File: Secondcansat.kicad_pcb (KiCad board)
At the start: 2 copper layers, 80 x 80 mm, 53 parts, among them IC1 XBP9B-XCWT-001, J1 OpenlogBreakout, J2 camerapower, J3 Pressure_MS5607, J4 Debugger, J5 light_sensor__SFH 7776, J6 CAM-M8Q-GPS, Q1 Q_PMOS_DGS, Q2 Q_NMOS_DGS, Q3 Q_NMOS_DGS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

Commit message: Finish PCB
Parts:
- moved C4 1.69 mm to (90.4, 107.1)
- moved L1 0.76 mm to (86.3, 108.3)
- moved C5 0.75 mm to (89.8, 109.1)
- moved L2 0.75 mm to (84.2, 108.3)
- moved C1 0.61 mm to (88.3, 111.4)
- moved R11 0.57 mm to (66.8, 85.4), turned to 0 degrees
- moved C2 0.38 mm to (88.5, 113.3)
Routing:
- net +3V3: track 0.00 -> 153.5 mm, vias 0 -> 6
- net +6V: track 0.00 -> 39.2 mm, vias 0 -> 3
- net SCL: track 0.00 -> 25.9 mm
- net SDA: track 0.00 -> 25.8 mm
- net TC_PD0: track 0.00 -> 17.7 mm, vias 0 -> 2
- net +5V: track 0.00 -> 15.8 mm
- net CSB: track 0.00 -> 13.6 mm
- net MCUVCC: track 0.00 -> 11.3 mm
- net Net-(C12-Pad2): track 0.00 -> 9.30 mm
- net MISO: track 0.00 -> 7.48 mm
- net Net-(C12-Pad1): track 0.00 -> 7.25 mm
- net SCLK: track 0.00 -> 6.83 mm
- net Net-(R1-Pad2): track 0.00 -> 6.37 mm
- net Net-(Q2-Pad3): track 0.00 -> 6.08 mm
- net PDICLK: track 0.00 -> 5.52 mm
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
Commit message: the real PCB
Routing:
- net GND: track 0.00 -> 124.5 mm, vias 0 -> 11
- net PDICLK: track 5.52 -> 61.4 mm, vias 0 -> 2
- net +6V: track 39.2 -> 90.6 mm, vias 3 -> 4
- net Therm_ADCA0: track 0.00 -> 47.7 mm, vias 0 -> 4
- net +3V3: track 153.5 -> 197.0 mm, vias 6 -> 7
- net PDIDATA: track 0.00 -> 38.2 mm, vias 0 -> 1
- net TX_PD7: track 0.00 -> 36.6 mm, vias 0 -> 2
- net RX_PD6: track 0.00 -> 33.3 mm, vias 0 -> 2
- net ADC_A1: track 0.00 -> 30.6 mm, vias 0 -> 2
- net MCUAVCC: track 4.50 -> 31.7 mm, vias 0 -> 2
- net SDA: track 25.8 -> 51.0 mm
- net PWM: track 1.63 -> 24.3 mm, vias 0 -> 2
- net MoterRIN1: track 1.88 -> 21.5 mm, vias 0 -> 2
- net MoterRIN2: track 0.00 -> 19.5 mm, vias 0 -> 2
- net MotorFIN1: track 0.00 -> 18.5 mm, vias 0 -> 2
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- added copper zone on B.Cu, net GND
- added copper zone on F.Cu, net GND

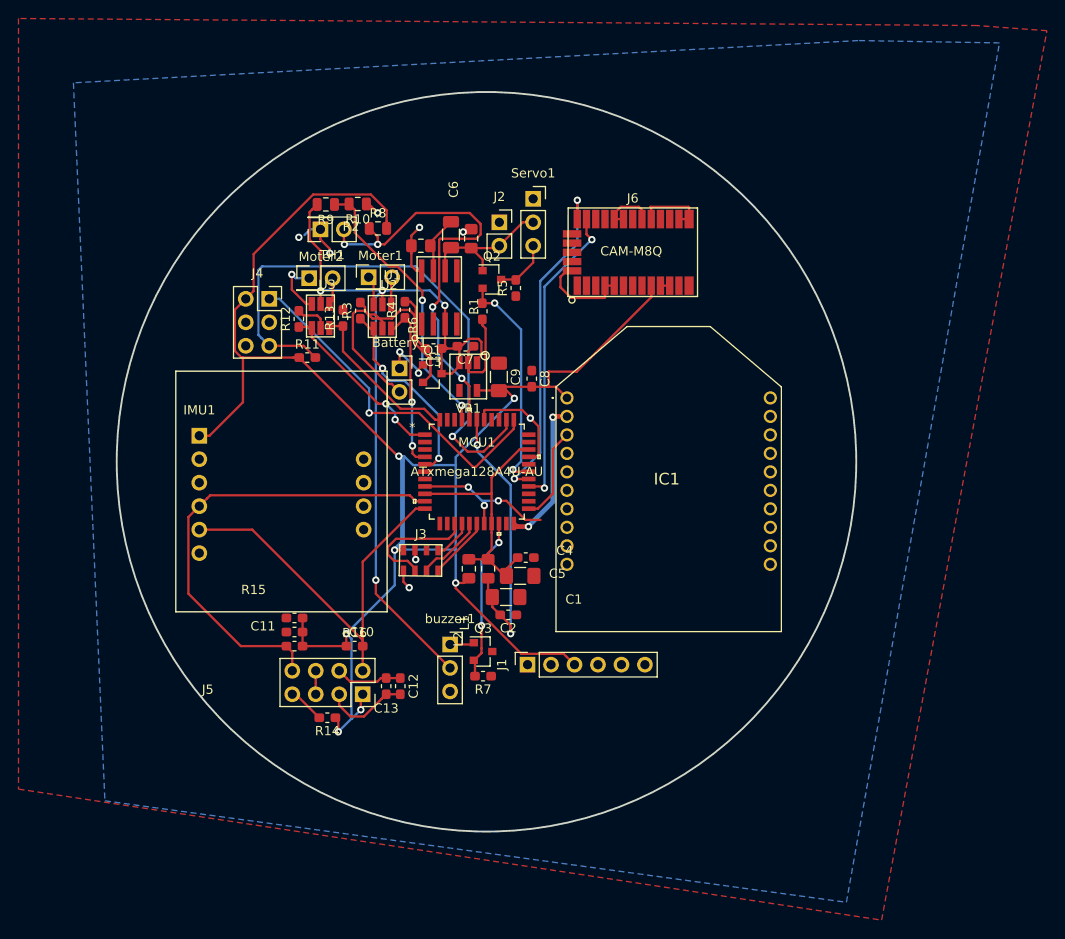
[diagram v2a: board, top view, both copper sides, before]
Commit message: moved reference values, added no fill zone and removed extra pin on moter
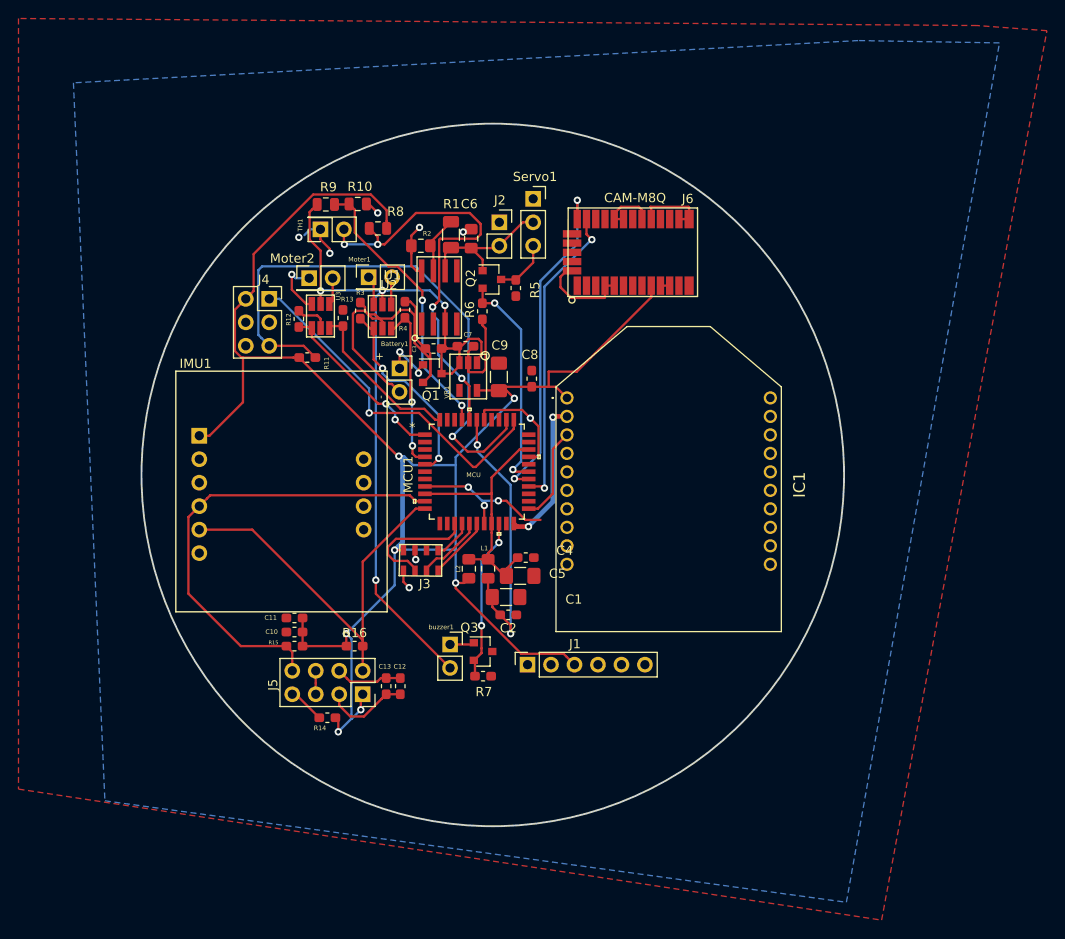
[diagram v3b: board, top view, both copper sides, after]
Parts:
- MCU1: value ATxmega128A4U-AU -> MCU
- buzzer1: footprint Connector_PinSocket_2.54mm:PinSocket_1x03_P2.54mm_Vertical -> Connector_PinSocket_2.54mm:PinSocket_1x02_P2.54mm_Vertical
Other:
- board size 80 x 80 mm -> 76 x 76 mm
- board text added: "+"
- board text added: "-"

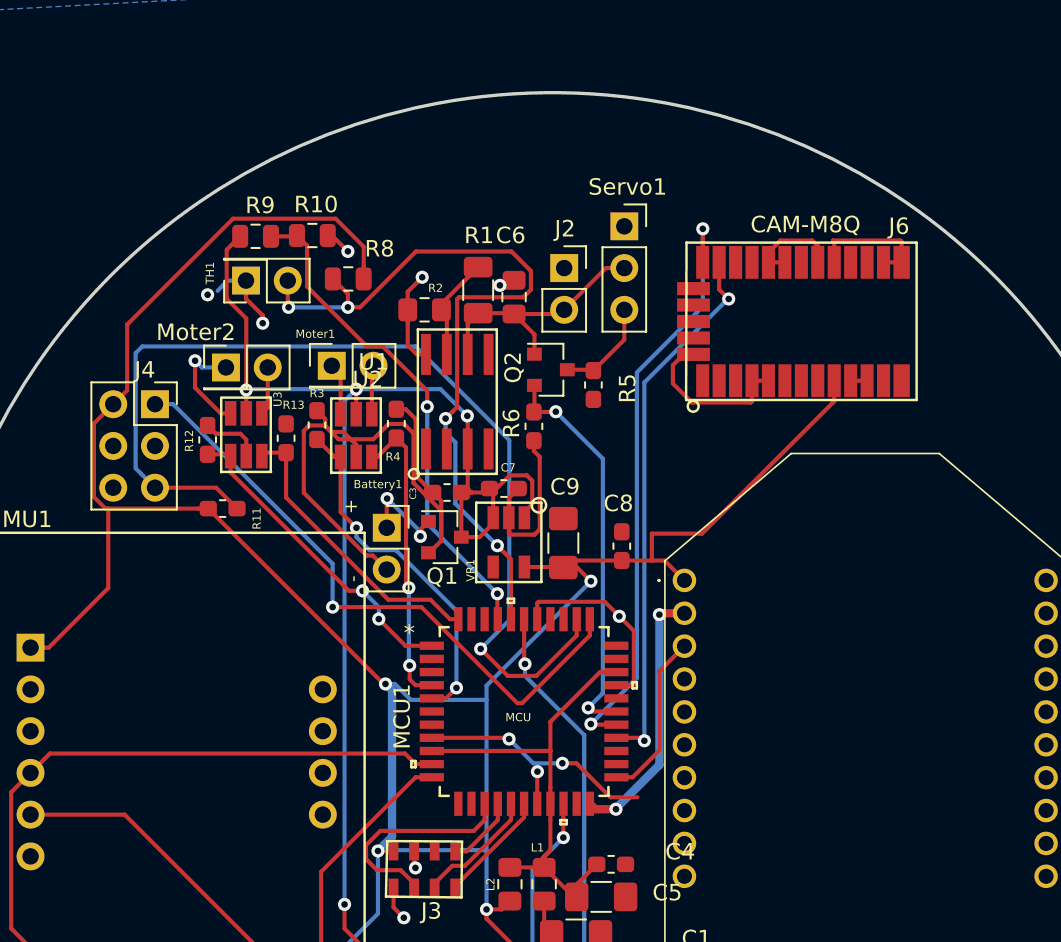
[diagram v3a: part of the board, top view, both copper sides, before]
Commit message: added prototype pins
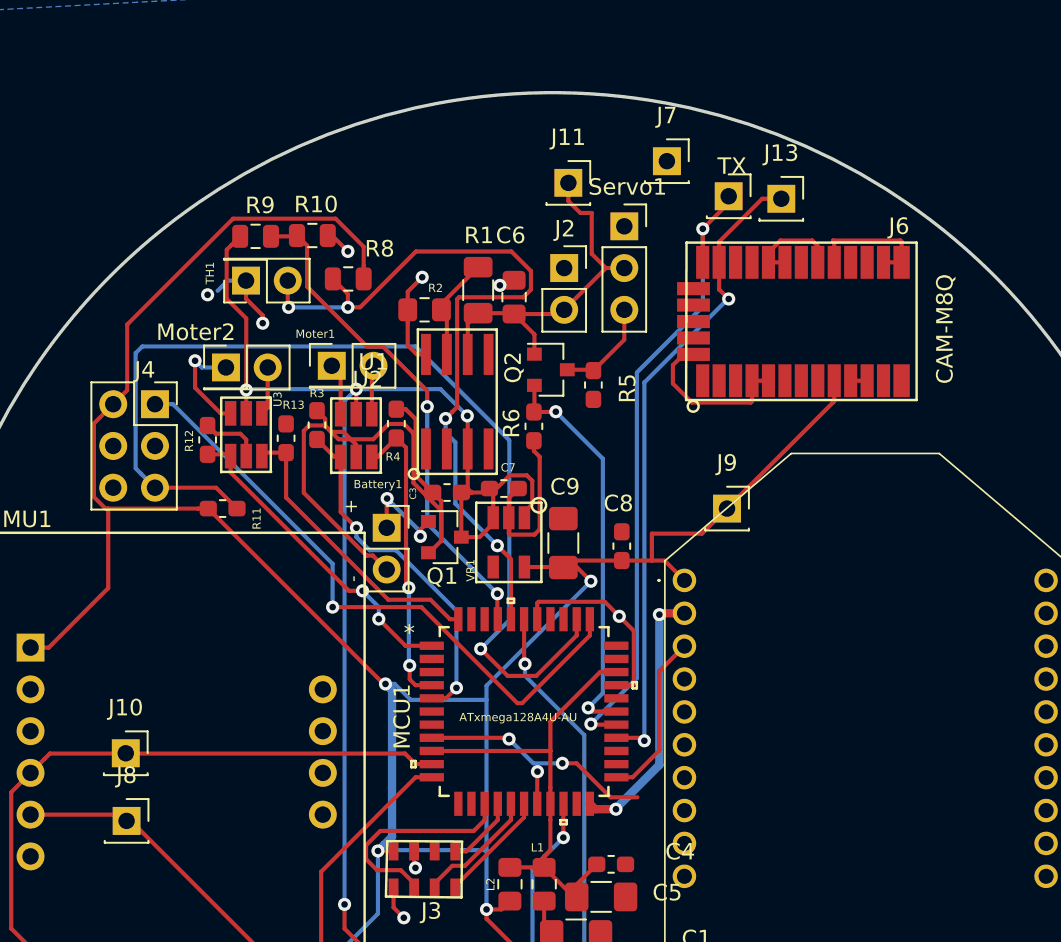
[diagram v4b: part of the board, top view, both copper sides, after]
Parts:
- added J10: SDA, Connector_PinSocket_2.54mm:PinSocket_1x01_P2.54mm_Vertical, F.Cu at (60.9, 100.3)
- added J11: 5V, Connector_PinSocket_2.54mm:PinSocket_1x01_P2.54mm_Vertical, F.Cu at (87.8, 65.6)
- added J13: Rx, Connector_PinSocket_2.54mm:PinSocket_1x01_P2.54mm_Vertical, F.Cu at (100.7, 66.6)
- added J7: GND, Connector_PinSocket_2.54mm:PinSocket_1x01_P2.54mm_Vertical, F.Cu at (93.8, 64.3)
- added J8: SCL, Connector_PinSocket_2.54mm:PinSocket_1x01_P2.54mm_Vertical, F.Cu at (60.9, 104.4)
- added J9: 3v, Connector_PinSocket_2.54mm:PinSocket_1x01_P2.54mm_Vertical, F.Cu at (97.4, 85.4)
- added TX: Tx, Connector_PinSocket_2.54mm:PinSocket_1x01_P2.54mm_Vertical, F.Cu at (97.5, 66.4)
- MCU1: value MCU -> ATxmega128A4U-AU
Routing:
- net +5V: track 15.8 -> 22.3 mm
- net RX_PD6: track 33.3 -> 39.4 mm
- net TX_PD7: track 36.6 -> 39.2 mm

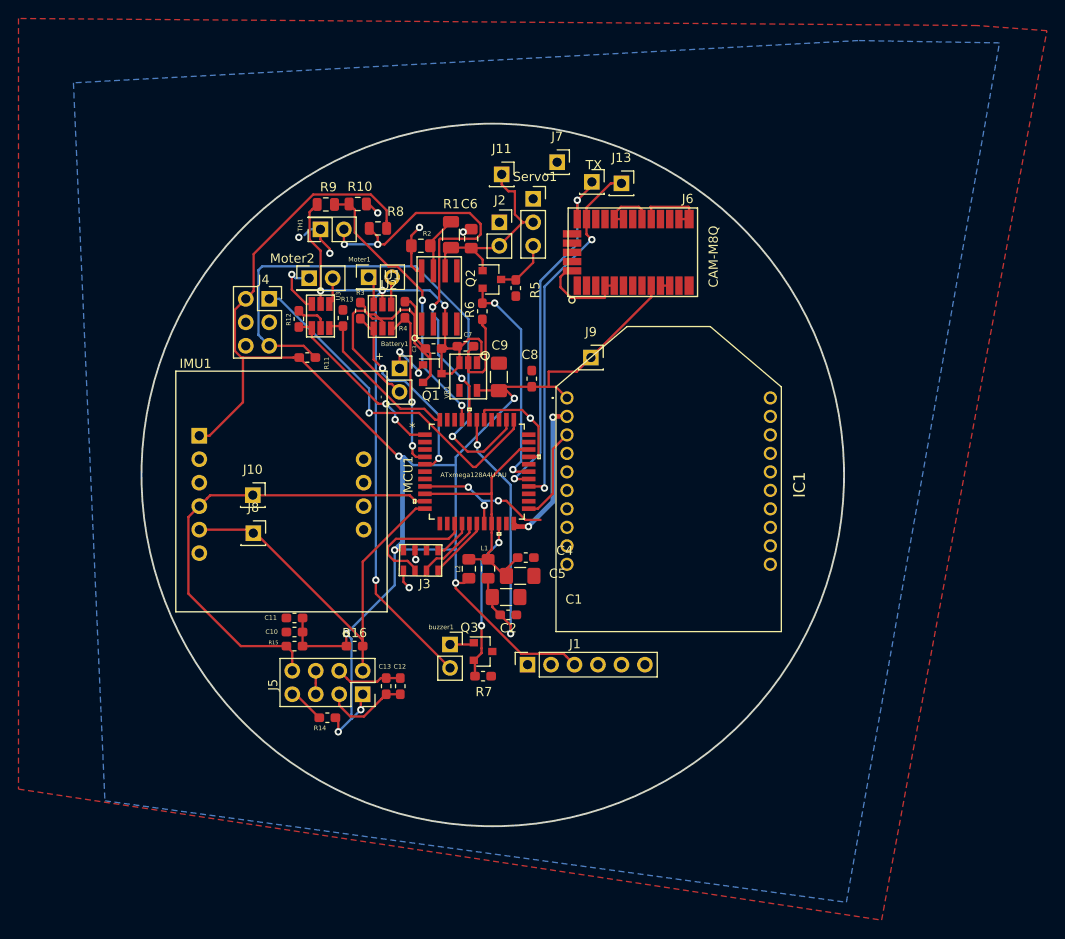
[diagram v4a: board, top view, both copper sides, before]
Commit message: Made some fixes to the PCB and footprint
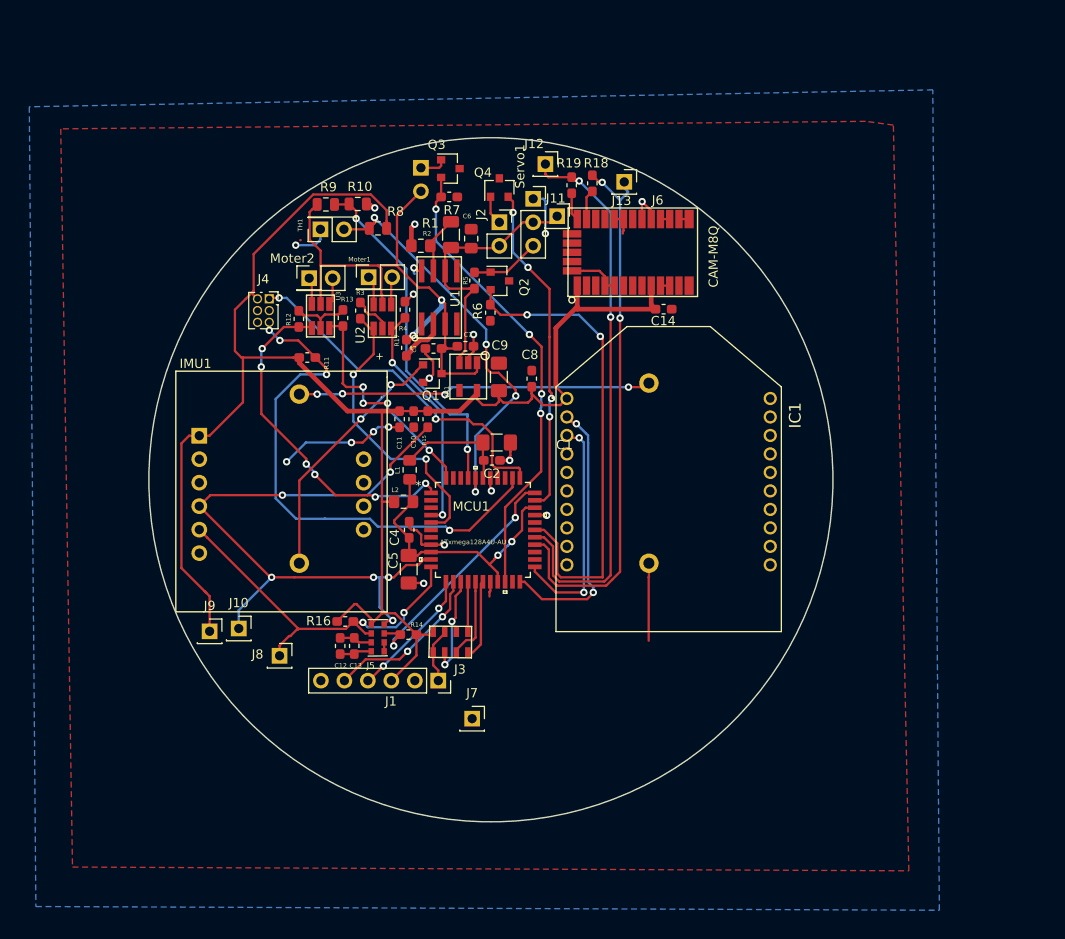
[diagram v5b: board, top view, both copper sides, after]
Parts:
- removed Battery1: battery, Connector_PinSocket_2.54mm:PinSocket_1x02_P2.54mm_Vertical
- removed TX: Tx, Connector_PinSocket_2.54mm:PinSocket_1x01_P2.54mm_Vertical
- added C14: 5uF, Capacitor_SMD:C_0603_1608Metric_Pad1.05x0.95mm_HandSolder, F.Cu at (105.3, 80.2)
- added J12: Tx, Connector_PinSocket_2.54mm:PinSocket_1x01_P2.54mm_Vertical, F.Cu at (92.5, 64.5)
- added J14: Battery_Holder_keystone 1079, CanSAT2ndtry:BatteryHolder, B.Cu at (84.8, 98.6)
- added Q4: Q_NMOS_BSS138, Package_TO_SOT_SMD:SOT-23, F.Cu at (87.5, 67.1)
- added R17: 10kohm, Resistor_SMD:R_0603_1608Metric_Pad1.05x0.95mm_HandSolder, F.Cu at (77.5, 84.4)
- added R18: 220ohm, Resistor_SMD:R_0603_1608Metric_Pad1.05x0.95mm_HandSolder, F.Cu at (97.6, 66.6)
- added R19: 220ohm, Resistor_SMD:R_0603_1608Metric_Pad1.05x0.95mm_HandSolder, F.Cu at (95.4, 66.8)
- C1, C5: value CP1 -> 10uF
- C2: value C -> 100nF
- IC1: footprint CanSAT2ndtry:XBP9BXCWT001 -> CanSAT2ndtry:XBP9BXCWT001_2
- J4: footprint Connector_PinSocket_2.54mm:PinSocket_2x03_P2.54mm_Vertical -> Connector_PinSocket_1.27mm:PinSocket_2x03_P1.27mm_Vertical
- J5: value light_sensor__SFH 7776 -> SFH_7776_OSRAM; footprint Connector_PinSocket_2.54mm:PinSocket_2x04_P2.54mm_Vertical -> CanSAT2ndtry:SFH7776
- L1, L2: value INDUCTOR -> 10uH
- Q1: value Q_PMOS_DGS -> Q_PMOS_DMG2305UX-13DIDKR-ND
- Q2, Q3: value Q_NMOS_DGS -> Q_NMOS_BSS138
- TH1: value Thermistor -> Therm_NXRT15WB473FA3A016
- buzzer1: value buzzer -> buzzer_MAS803Q; moved to B.Cu
- moved J7 60.9 mm to (84.6, 124.5)
- moved Q3 52.4 mm to (82.2, 65.0)
- moved R7 52.0 mm to (82.1, 68.1)
- moved buzzer1 51.7 mm to (79.0, 64.9), turned to 180 degrees
- moved J9 50.8 mm to (56.2, 115.1)
- moved R15 28.5 mm to (79.8, 92.1), turned to 270 degrees
- moved C10 26.4 mm to (78.3, 92.1), turned to 270 degrees
- moved C11 24.3 mm to (76.7, 92.1), turned to 270 degrees
- moved C2 16.8 mm to (86.7, 96.6)
- moved C1 16.7 mm to (87.2, 94.6)
- moved J10 14.5 mm to (59.3, 114.8)
- moved L1 13.7 mm to (77.8, 97.6), turned to 270 degrees
- moved J8 13.6 mm to (63.8, 117.7)
- moved C4 13.0 mm to (77.8, 104.1), turned to 270 degrees
- moved R14 12.6 mm to (77.7, 115.4)
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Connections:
- J1 pad 4: RX_OPenlog_PC2 -> USART_RX_PC2
- J1 pad 5: TX_openlog_PC3 -> USART_TX_PC3
- J2 pad 1: GND -> Net-(J2-Pad1)
- J5 pad 7: Net-(J5-Pad7) -> INT
- J6 pad 1: Net-(J6-Pad1) -> +3V3
- J6 pad 17: Net-(J6-Pad17) -> Net-(J6-Pad16)
- J6 pad 25: RX_PD6 -> Net-(J6-Pad25)
- J6 pad 26: TX_PD7 -> Net-(J6-Pad26)
- MCU1 pad 32: Net-(MCU1-Pad32) -> cameraon
- MCU1 pad 33: Net-(MCU1-Pad33) -> INT
- Q2 pad 1: +5V -> Net-(Q2-Pad1)
- Q2 pad 3: Net-(Q2-Pad3) -> GND
- R14 pad 2: Net-(J5-Pad7) -> INT
- R5 pad 1: GND -> +5V
- R5 pad 2: Net-(Q2-Pad3) -> Net-(Q2-Pad1)
- Servo1 pad 3: Net-(Q2-Pad3) -> Net-(Q2-Pad1)
- VR1 pad 3: +6V -> +5V
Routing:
- net Net-(J14-Pad1): track 0.00 -> 38.4 mm, vias 0 -> 4
- net cameraon: track 0.00 -> 36.1 mm, vias 0 -> 4
- net TC_PD0: track 17.7 -> 51.0 mm, vias 2 -> 4
- net GND: track 124.5 -> 92.6 mm, vias 11 -> 18
- net +6V: track 90.6 -> 60.7 mm, vias 4 -> 2
- net PWM: track 24.3 -> 52.5 mm
- net INT: track 0.00 -> 26.8 mm, vias 0 -> 2
- net TX_PD7: track 39.2 -> 61.4 mm
- net Net-(J14-Pad4): track 6.03 -> 27.8 mm
- net RX_PD6: track 39.4 -> 60.3 mm
- net SDA: track 51.0 -> 71.2 mm, vias 0 -> 6
- net MCUAVCC: track 31.7 -> 12.6 mm, vias 2 -> 0
- net MoterRIN2: track 19.5 -> 37.2 mm, vias 2 -> 6
- net USART_TX_PC3: track 0.00 -> 17.7 mm, vias 0 -> 2
- net TX_PD3: track 10.3 -> 25.1 mm, vias 0 -> 2
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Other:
- board size 76 x 76 mm -> 74 x 74 mm

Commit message: fixed PCB
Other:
- outline, holes or cut-outs redrawn
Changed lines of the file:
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@@
   (general
     (thickness 1.6)
-    (drawings 3)
+    (drawings 5)
     (tracks 709)
     (zones 0)
@@
   )
   (setup
-    (last_trace_width 0.254)
+    (last_trace_width 0.25)
     (user_trace_width 0.254)
     (user_trace_width 0.508)
@@
     )
   )
+  (gr_circle (center 112.5728 77.8764) (end 115.1128 79.2988) (layer Edge.Cuts) (width 0.15))
+  (gr_circle (center 87.106446 130.302) (end 89.646446 131.7244) (layer Edge.Cuts) (width 0.15))
   (gr_circle (center 86.614 98.6712) (end 123.614 98.6712) (layer Edge.Cuts) (width 0.15))
   (gr_text - (at 74.676 89.7128 90) (layer F.SilkS)
@@
   (segment (start 81.0196 64.9224) (end 81.2292 64.7128) (width 0.254) (layer F.Cu) (net 2))
   (segment (start 79.0448 64.9224) (end 81.0196 64.9224) (width 0.254) (layer F.Cu) (net 2))
-  (segment (start 80.87 65.9384) (end 81.058 65.7504) (width 0.254) (layer F.Cu) (net 67))
   (segment (start 68.1888 79.6544) (end 68.1888 78.232) (width 0.25) (layer F.Cu) (net 3))
   (segment (start 68.1888 73.877402) (end 66.998599 72.687201) (width 0.25) (layer F.Cu) (net 3))
@@
   (segment (start 82.20441 112.660568) (end 82.20441 111.039191) (width 0.254) (layer F.Cu) (net 66))
   (segment (start 81.376019 113.488959) (end 82.20441 112.660568) (width 0.254) (layer F.Cu) (net 66))
+  (segment (start 80.87 65.9384) (end 81.058 65.7504) (width 0.254) (layer F.Cu) (net 67))
   (segment (start 81.2292 65.9588) (end 81.2292 68.072) (width 0.254) (layer F.Cu) (net 67))
   (segment (start 88.1504 109.7026) (end 88.1504 101.655002) (width 0.254) (layer F.Cu) (net 67))
